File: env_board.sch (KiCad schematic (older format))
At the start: 8 parts, among them J1 CONN_01X07, U1 RFD77101, U2 ENS210, U3 CCS811

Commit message: update schematics
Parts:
- removed R1: 10k, Resistors_SMD:R_0603, symbol R
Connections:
- net BATT_V_EN: now also U1.11 (P0.19); no longer U1.20 (P0.08)
- net CCS_WAKE: now also U1.28 (P0.13)
- net VDD: now also U3.2 (~RESET); no longer J1.3 (P3)
- new net VBUS: J1.3 (P3)
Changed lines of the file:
@@
 $EndComp
 $Comp
-L VDD #PWR09
-U 1 1 599D616B
-P 3100 1900
-F 0 "#PWR09" H 3100 1750 50  0001 C CNN
-F 1 "VDD" H 3100 2050 50  0000 C CNN
-F 2 "" H 3100 1900 50  0001 C CNN
-F 3 "" H 3100 1900 50  0001 C CNN
-	1    3100 1900
-	1    0    0    -1
-$EndComp
-$Comp
-L GND #PWR010
+L GND #PWR09
 U 1 1 599D619D
 P 2550 2250
-F 0 "#PWR010" H 2550 2000 50  0001 C CNN
+F 0 "#PWR09" H 2550 2000 50  0001 C CNN
 F 1 "GND" H 2550 2100 50  0000 C CNN
 F 2 "" H 2550 2250 50  0001 C CNN
@@
 CCS_INT
 Wire Wire Line
-	9300 3050 9200 3050
-Wire Wire Line
-	9200 3050 9200 2750
-Wire Wire Line
 	8900 2750 10400 2750
 Connection ~ 9700 2750
@@
 Text Label 9300 3650 2    60   ~ 0
 CCS_WAKE
-$Comp
-L R R1
-U 1 1 599D70BF
-P 8900 3250
-F 0 "R1" V 8980 3250 50  0000 C CNN
-F 1 "10k" V 8900 3250 50  0000 C CNN
-F 2 "Resistors_SMD:R_0603" V 8830 3250 50  0001 C CNN
-F 3 "" H 8900 3250 50  0001 C CNN
-	1    8900 3250
-	1    0    0    -1
-$EndComp
 Wire Wire Line
-	9300 3550 8900 3550
+	8900 3550 9300 3550
 Wire Wire Line
-	8900 3550 8900 3400
-Wire Wire Line
-	8900 3100 8900 2750
-Connection ~ 9200 2750
+	8900 2750 8900 3550
 NoConn ~ 10100 3450
 $Comp
@@
 $EndComp
 $Comp
-L GND #PWR011
+L GND #PWR010
 U 1 1 599D736D
 P 10400 3050
-F 0 "#PWR011" H 10400 2800 50  0001 C CNN
+F 0 "#PWR010" H 10400 2800 50  0001 C CNN
 F 1 "GND" H 10400 2900 50  0000 C CNN
 F 2 "" H 10400 3050 50  0001 C CNN
@@
 Text Label 2700 3250 0    60   ~ 0
 BATT_V_EN
-Text Label 4050 4350 2    60   ~ 0
+Text Label 5450 4150 0    60   ~ 0
 BATT_V_EN
 Text Label 4050 3850 2    60   ~ 0
@@
 Text Label 4050 3250 2    60   ~ 0
 SWDIO/RESET
+$Comp
+L VBUS #PWR011
+U 1 1 59F89288
+P 3100 1900
+F 0 "#PWR011" H 3100 1750 50  0001 C CNN
+F 1 "VBUS" H 3100 2050 50  0000 C CNN
+F 2 "" H 3100 1900 50  0001 C CNN
+F 3 "" H 3100 1900 50  0001 C CNN
+	1    3100 1900
+	1    0    0    -1
+$EndComp
+Text Label 4050 4850 2    60   ~ 0
+CCS_WAKE
+Wire Wire Line
+	9300 3050 9100 3050
+Wire Wire Line
+	9100 3050 9100 2750
+Connection ~ 9100 2750
 $EndSCHEMATC

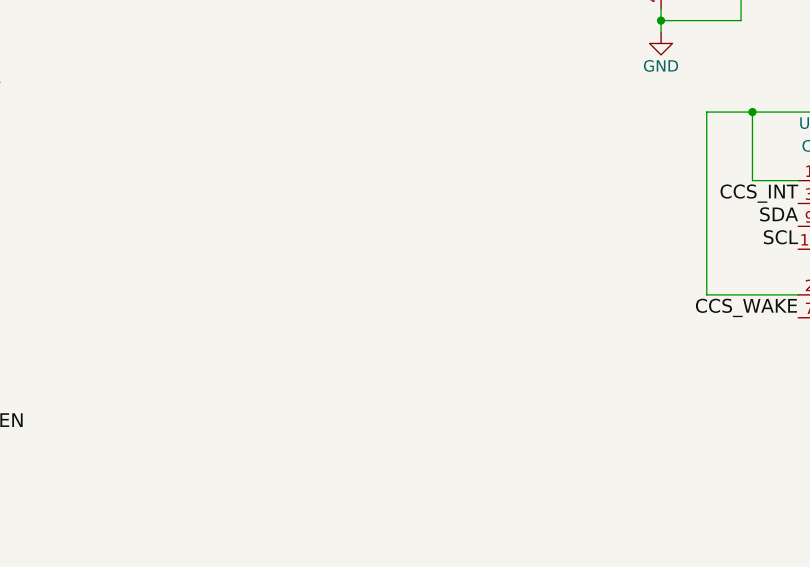
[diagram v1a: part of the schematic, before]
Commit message: update board, schematics, add bmp280
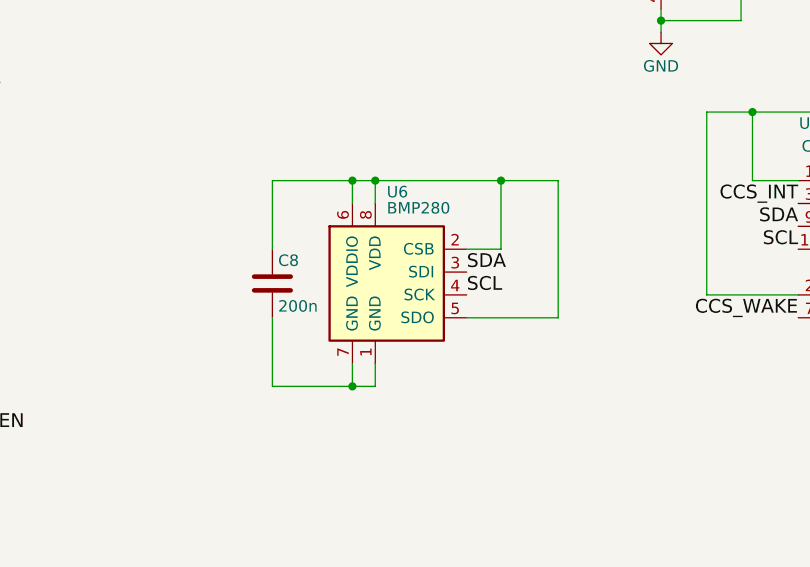
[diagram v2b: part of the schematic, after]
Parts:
- added C8: 200n, Capacitors_SMD:C_0603, symbol C
- added U6: BMP280, Housings_LGA:Bosch_LGA-8_2x2.5mm_Pitch0.65mm, symbol BMP280
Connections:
- net SCL: now also U6.4 (SCK)
- net SDA: now also U6.3 (SDI)
- new net: C8.2, U6.1 (GND), U6.7 (GND)
- new net: C8.1, U6.2 (CSB), U6.5 (SDO), U6.6 (VDDIO), U6.8 (VDD)
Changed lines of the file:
@@
 EESchema Schematic File Version 2
+LIBS:env_board-rescue
 LIBS:power
 LIBS:device
@@
 $EndComp
 $Comp
-L GND #PWR01
+L GND #PWR3
 U 1 1 596DD545
 P 4650 5550
-F 0 "#PWR01" H 4650 5300 50  0001 C CNN
+F 0 "#PWR3" H 4650 5300 50  0001 C CNN
 F 1 "GND" H 4650 5400 50  0000 C CNN
 F 2 "" H 4650 5550 50  0001 C CNN
@@
 $EndComp
 $Comp
-L VDD #PWR02
+L VDD #PWR4
 U 1 1 596DD567
 P 4750 2750
-F 0 "#PWR02" H 4750 2600 50  0001 C CNN
+F 0 "#PWR4" H 4750 2600 50  0001 C CNN
 F 1 "VDD" H 4750 2900 50  0000 C CNN
 F 2 "" H 4750 2750 50  0001 C CNN
@@
 $EndComp
 $Comp
-L VDD #PWR03
+L VDD #PWR5
 U 1 1 596DD6D5
 P 5700 2550
-F 0 "#PWR03" H 5700 2400 50  0001 C CNN
+F 0 "#PWR5" H 5700 2400 50  0001 C CNN
 F 1 "VDD" H 5700 2700 50  0000 C CNN
 F 2 "" H 5700 2550 50  0001 C CNN
@@
 $EndComp
 $Comp
-L GND #PWR04
+L GND #PWR6
 U 1 1 596DD6F2
 P 5700 2850
-F 0 "#PWR04" H 5700 2600 50  0001 C CNN
+F 0 "#PWR6" H 5700 2600 50  0001 C CNN
 F 1 "GND" H 5700 2700 50  0000 C CNN
 F 2 "" H 5700 2850 50  0001 C CNN
@@
 $EndComp
 $Comp
-L VDD #PWR05
+L VDD #PWR7
 U 1 1 599D59B0
 P 8700 1600
-F 0 "#PWR05" H 8700 1450 50  0001 C CNN
+F 0 "#PWR7" H 8700 1450 50  0001 C CNN
 F 1 "VDD" H 8700 1750 50  0000 C CNN
 F 2 "" H 8700 1600 50  0001 C CNN
@@
 $EndComp
 $Comp
-L GND #PWR06
+L GND #PWR8
 U 1 1 599D59DF
 P 8700 2400
-F 0 "#PWR06" H 8700 2150 50  0001 C CNN
+F 0 "#PWR8" H 8700 2150 50  0001 C CNN
 F 1 "GND" H 8700 2250 50  0000 C CNN
 F 2 "" H 8700 2400 50  0001 C CNN
@@
 	8700 2300 8700 2400
 $Comp
-L VDD #PWR07
+L VDD #PWR9
 U 1 1 599D5AF3
 P 9700 2700
-F 0 "#PWR07" H 9700 2550 50  0001 C CNN
+F 0 "#PWR9" H 9700 2550 50  0001 C CNN
 F 1 "VDD" H 9700 2850 50  0000 C CNN
 F 2 "" H 9700 2700 50  0001 C CNN
@@
 $EndComp
 $Comp
-L GND #PWR08
+L GND #PWR10
 U 1 1 599D5B22
 P 9700 3900
-F 0 "#PWR08" H 9700 3650 50  0001 C CNN
+F 0 "#PWR10" H 9700 3650 50  0001 C CNN
 F 1 "GND" H 9700 3750 50  0000 C CNN
 F 2 "" H 9700 3900 50  0001 C CNN
@@
 $EndComp
 $Comp
-L GND #PWR09
+L GND #PWR1
 U 1 1 599D619D
 P 2550 2250
-F 0 "#PWR09" H 2550 2000 50  0001 C CNN
+F 0 "#PWR1" H 2550 2000 50  0001 C CNN
 F 1 "GND" H 2550 2100 50  0000 C CNN
 F 2 "" H 2550 2250 50  0001 C CNN
@@
 $EndComp
 $Comp
-L GND #PWR010
+L GND #PWR11
 U 1 1 599D736D
 P 10400 3050
-F 0 "#PWR010" H 10400 2800 50  0001 C CNN
+F 0 "#PWR11" H 10400 2800 50  0001 C CNN
 F 1 "GND" H 10400 2900 50  0000 C CNN
 F 2 "" H 10400 3050 50  0001 C CNN
@@
 SWDIO/RESET
 $Comp
-L VBUS #PWR011
+L VBUS #PWR2
 U 1 1 59F89288
 P 3100 1900
-F 0 "#PWR011" H 3100 1750 50  0001 C CNN
+F 0 "#PWR2" H 3100 1750 50  0001 C CNN
 F 1 "VBUS" H 3100 2050 50  0000 C CNN
 F 2 "" H 3100 1900 50  0001 C CNN
@@
 	9100 3050 9100 2750
 Connection ~ 9100 2750
+$Comp
+L BMP280 U6
+U 1 1 5A01D7B2
+P 7450 3450
+F 0 "U6" H 7500 3800 50  0000 L CNN
+F 1 "BMP280" H 7500 3700 50  0000 L BNN
+F 2 "Housings_LGA:Bosch_LGA-8_2x2.5mm_Pitch0.65mm" H 7350 3450 50  0001 C CNN
+F 3 "" H 7350 3450 50  0001 C CNN
+	1    7450 3450
+	1    0    0    -1
+$EndComp
+$Comp
+L C C8
+U 1 1 5A01D9B5
+P 7000 3500
+F 0 "C8" H 7025 3600 50  0000 L CNN
+F 1 "200n" H 7025 3400 50  0000 L CNN
+F 2 "Capacitors_SMD:C_0603" H 7038 3350 50  0001 C CNN
+F 3 "" H 7000 3500 50  0001 C CNN
+	1    7000 3500
+	1    0    0    -1
+$EndComp
+Wire Wire Line
+	7000 3350 7000 3050
+Wire Wire Line
+	7000 3050 8250 3050
+Wire Wire Line
+	7450 3050 7450 3150
+Wire Wire Line
+	7350 3150 7350 3050
+Connection ~ 7350 3050
+Wire Wire Line
+	7000 3650 7000 3950
+Wire Wire Line
+	7000 3950 7450 3950
+Wire Wire Line
+	7450 3950 7450 3850
+Wire Wire Line
+	7350 3850 7350 3950
+Connection ~ 7350 3950
+Wire Wire Line
+	7850 3650 8250 3650
+Wire Wire Line
+	8250 3650 8250 3050
+Connection ~ 7450 3050
+Wire Wire Line
+	7850 3350 8000 3350
+Wire Wire Line
+	8000 3350 8000 3050
+Connection ~ 8000 3050
+Text Label 7850 3450 0    60   ~ 0
+SDA
+Text Label 7850 3550 0    60   ~ 0
+SCL
 $EndSCHEMATC

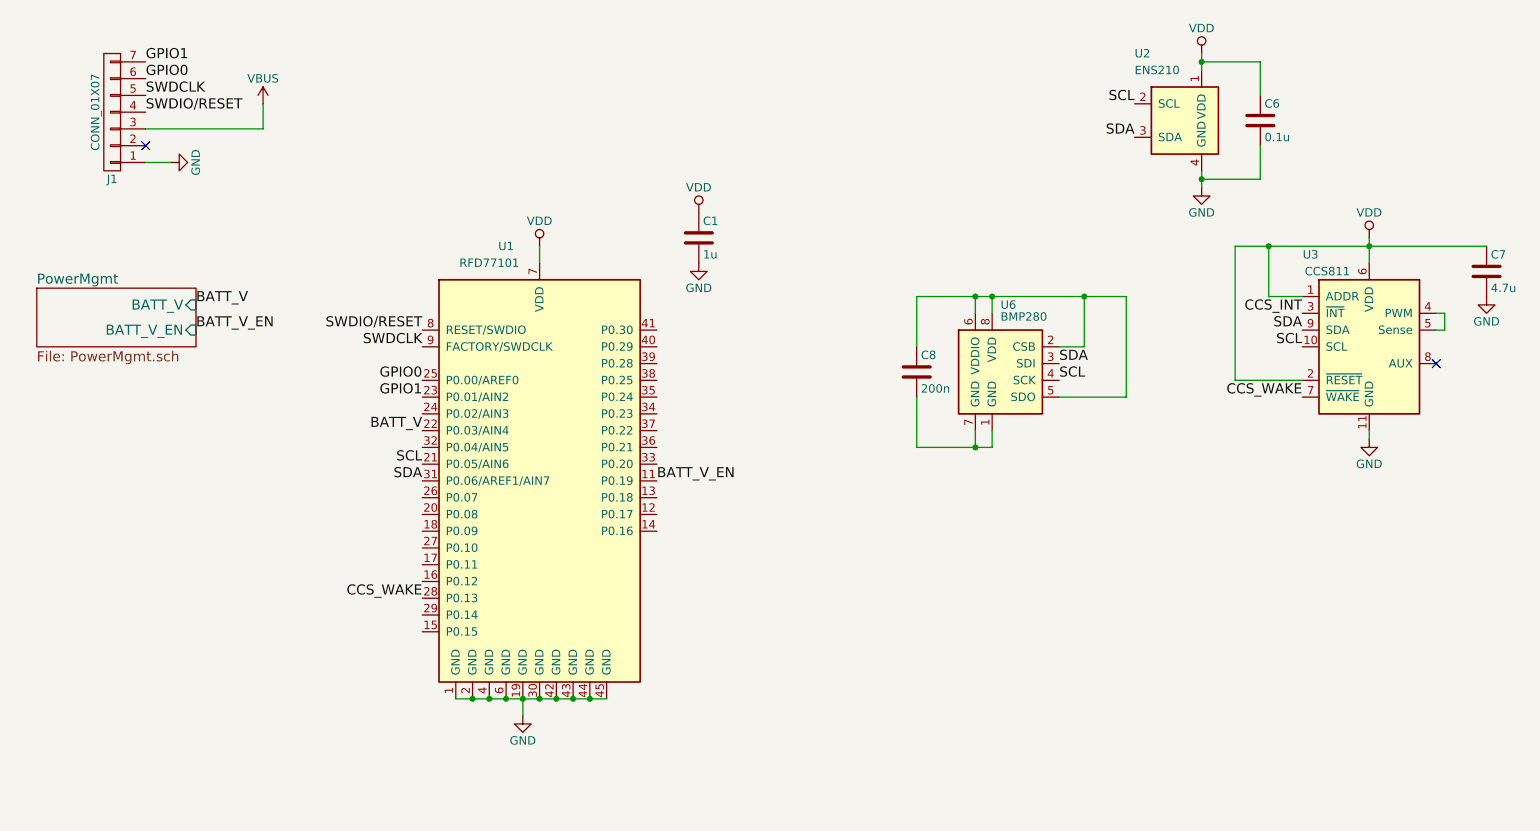
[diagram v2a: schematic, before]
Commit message: update sensor and add housing for sensor
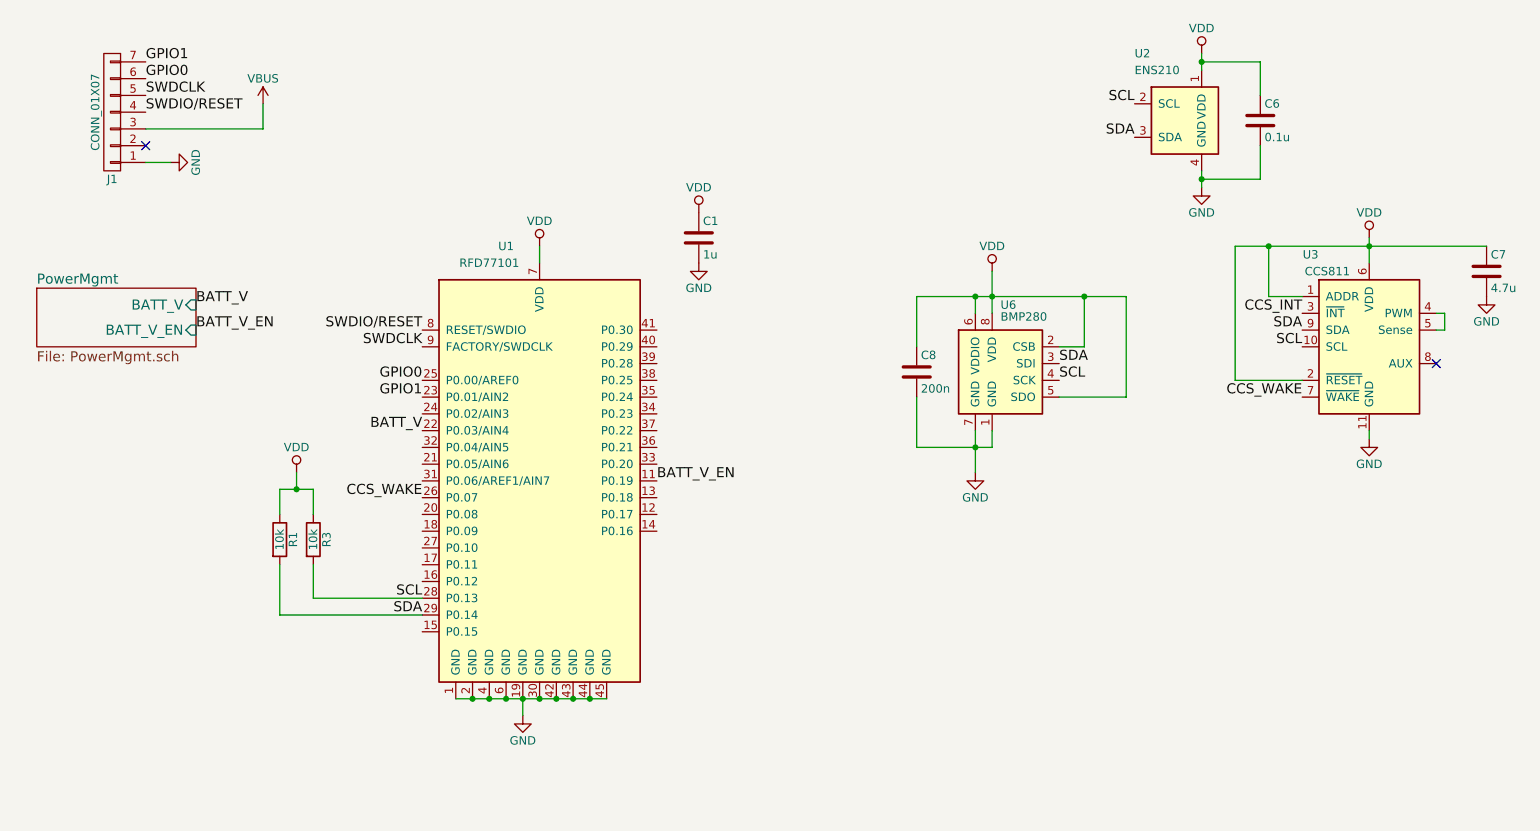
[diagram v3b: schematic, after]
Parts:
- added R1, R3: 10k, Resistors_SMD:R_0603, symbol R
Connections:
- net CCS_WAKE: now also U1.26 (P0.07); no longer U1.28 (P0.13)
- net GND: now also C8.2, U6.1 (GND), U6.7 (GND)
- net SCL: now also U1.28 (P0.13), R3.2; no longer U1.21 (P0.05/AIN6)
- net SDA: now also U1.29 (P0.14), R1.2; no longer U1.31 (P0.06/AREF1/AIN7)
- net VDD: now also C8.1, U6.2 (CSB), U6.5 (SDO), U6.6 (VDDIO), U6.8 (VDD), R1.1, R3.1
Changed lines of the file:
@@
 LIBS:rfcom
 LIBS:sensors
-LIBS:Battery_Management
 LIBS:env_board-cache
 EELAYER 25 0
@@
 $EndComp
 $Comp
-L GND #PWR3
+L GND #PWR01
 U 1 1 596DD545
 P 4650 5550
-F 0 "#PWR3" H 4650 5300 50  0001 C CNN
+F 0 "#PWR01" H 4650 5300 50  0001 C CNN
 F 1 "GND" H 4650 5400 50  0000 C CNN
 F 2 "" H 4650 5550 50  0001 C CNN
@@
 $EndComp
 $Comp
-L VDD #PWR4
+L VDD #PWR02
 U 1 1 596DD567
 P 4750 2750
-F 0 "#PWR4" H 4750 2600 50  0001 C CNN
+F 0 "#PWR02" H 4750 2600 50  0001 C CNN
 F 1 "VDD" H 4750 2900 50  0000 C CNN
 F 2 "" H 4750 2750 50  0001 C CNN
@@
 $EndComp
 $Comp
-L VDD #PWR5
+L VDD #PWR03
 U 1 1 596DD6D5
 P 5700 2550
-F 0 "#PWR5" H 5700 2400 50  0001 C CNN
+F 0 "#PWR03" H 5700 2400 50  0001 C CNN
 F 1 "VDD" H 5700 2700 50  0000 C CNN
 F 2 "" H 5700 2550 50  0001 C CNN
@@
 $EndComp
 $Comp
-L GND #PWR6
+L GND #PWR04
 U 1 1 596DD6F2
 P 5700 2850
-F 0 "#PWR6" H 5700 2600 50  0001 C CNN
+F 0 "#PWR04" H 5700 2600 50  0001 C CNN
 F 1 "GND" H 5700 2700 50  0000 C CNN
 F 2 "" H 5700 2850 50  0001 C CNN
@@
 $EndComp
 $Comp
-L VDD #PWR7
+L VDD #PWR05
 U 1 1 599D59B0
 P 8700 1600
-F 0 "#PWR7" H 8700 1450 50  0001 C CNN
+F 0 "#PWR05" H 8700 1450 50  0001 C CNN
 F 1 "VDD" H 8700 1750 50  0000 C CNN
 F 2 "" H 8700 1600 50  0001 C CNN
@@
 $EndComp
 $Comp
-L GND #PWR8
+L GND #PWR06
 U 1 1 599D59DF
 P 8700 2400
-F 0 "#PWR8" H 8700 2150 50  0001 C CNN
+F 0 "#PWR06" H 8700 2150 50  0001 C CNN
 F 1 "GND" H 8700 2250 50  0000 C CNN
 F 2 "" H 8700 2400 50  0001 C CNN
@@
 	8700 2300 8700 2400
 $Comp
-L VDD #PWR9
+L VDD #PWR07
 U 1 1 599D5AF3
 P 9700 2700
-F 0 "#PWR9" H 9700 2550 50  0001 C CNN
+F 0 "#PWR07" H 9700 2550 50  0001 C CNN
 F 1 "VDD" H 9700 2850 50  0000 C CNN
 F 2 "" H 9700 2700 50  0001 C CNN
@@
 $EndComp
 $Comp
-L GND #PWR10
+L GND #PWR08
 U 1 1 599D5B22
 P 9700 3900
-F 0 "#PWR10" H 9700 3650 50  0001 C CNN
+F 0 "#PWR08" H 9700 3650 50  0001 C CNN
 F 1 "GND" H 9700 3750 50  0000 C CNN
 F 2 "" H 9700 3900 50  0001 C CNN
@@
 $EndComp
 $Comp
-L GND #PWR1
+L GND #PWR09
 U 1 1 599D619D
 P 2550 2250
-F 0 "#PWR1" H 2550 2000 50  0001 C CNN
+F 0 "#PWR09" H 2550 2000 50  0001 C CNN
 F 1 "GND" H 2550 2100 50  0000 C CNN
 F 2 "" H 2550 2250 50  0001 C CNN
@@
 Text Label 4050 3650 2    60   ~ 0
 GPIO1
-Text Label 4050 4150 2    60   ~ 0
+Text Label 4050 4950 2    60   ~ 0
 SDA
-Text Label 4050 4050 2    60   ~ 0
+Text Label 4050 4850 2    60   ~ 0
 SCL
 Text Label 8300 2100 2    60   ~ 0
@@
 $EndComp
 $Comp
-L GND #PWR11
+L GND #PWR010
 U 1 1 599D736D
 P 10400 3050
-F 0 "#PWR11" H 10400 2800 50  0001 C CNN
+F 0 "#PWR010" H 10400 2800 50  0001 C CNN
 F 1 "GND" H 10400 2900 50  0000 C CNN
 F 2 "" H 10400 3050 50  0001 C CNN
@@
 SWDIO/RESET
 $Comp
-L VBUS #PWR2
+L VBUS #PWR011
 U 1 1 59F89288
 P 3100 1900
-F 0 "#PWR2" H 3100 1750 50  0001 C CNN
+F 0 "#PWR011" H 3100 1750 50  0001 C CNN
 F 1 "VBUS" H 3100 2050 50  0000 C CNN
 F 2 "" H 3100 1900 50  0001 C CNN
@@
 	1    0    0    -1
 $EndComp
-Text Label 4050 4850 2    60   ~ 0
+Text Label 4050 4250 2    60   ~ 0
 CCS_WAKE
 Wire Wire Line
@@
 	7000 3050 8250 3050
 Wire Wire Line
-	7450 3050 7450 3150
+	7450 2900 7450 3150
 Wire Wire Line
 	7350 3150 7350 3050
@@
 	7450 3950 7450 3850
 Wire Wire Line
-	7350 3850 7350 3950
+	7350 3850 7350 4100
 Connection ~ 7350 3950
 Wire Wire Line
@@
 Text Label 7850 3550 0    60   ~ 0
 SCL
+$Comp
+L VDD #PWR012
+U 1 1 5A71A152
+P 7450 2900
+F 0 "#PWR012" H 7450 2750 50  0001 C CNN
+F 1 "VDD" H 7450 3050 50  0000 C CNN
+F 2 "" H 7450 2900 50  0001 C CNN
+F 3 "" H 7450 2900 50  0001 C CNN
+	1    7450 2900
+	1    0    0    -1
+$EndComp
+$Comp
+L GND #PWR013
+U 1 1 5A71A1C7
+P 7350 4100
+F 0 "#PWR013" H 7350 3850 50  0001 C CNN
+F 1 "GND" H 7350 3950 50  0000 C CNN
+F 2 "" H 7350 4100 50  0001 C CNN
+F 3 "" H 7350 4100 50  0001 C CNN
+	1    7350 4100
+	1    0    0    -1
+$EndComp
+$Comp
+L R R3
+U 1 1 5A9016EB
+P 3400 4500
+F 0 "R3" V 3480 4500 50  0000 C CNN
+F 1 "10k" V 3400 4500 50  0000 C CNN
+F 2 "Resistors_SMD:R_0603" V 3330 4500 50  0001 C CNN
+F 3 "" H 3400 4500 50  0000 C CNN
+	1    3400 4500
+	1    0    0    -1
+$EndComp
+$Comp
+L R R1
+U 1 1 5A90189B
+P 3200 4500
+F 0 "R1" V 3280 4500 50  0000 C CNN
+F 1 "10k" V 3200 4500 50  0000 C CNN
+F 2 "Resistors_SMD:R_0603" V 3130 4500 50  0001 C CNN
+F 3 "" H 3200 4500 50  0000 C CNN
+	1    3200 4500
+	1    0    0    -1
+$EndComp
+Wire Wire Line
+	4050 4950 3200 4950
+Wire Wire Line
+	3200 4950 3200 4650
+Wire Wire Line
+	4050 4850 3400 4850
+Wire Wire Line
+	3400 4850 3400 4650
+$Comp
+L VDD #PWR014
+U 1 1 5A901B29
+P 3300 4100
+F 0 "#PWR014" H 3300 3950 50  0001 C CNN
+F 1 "VDD" H 3300 4250 50  0000 C CNN
+F 2 "" H 3300 4100 50  0001 C CNN
+F 3 "" H 3300 4100 50  0001 C CNN
+	1    3300 4100
+	1    0    0    -1
+$EndComp
+Wire Wire Line
+	3200 4350 3200 4200
+Wire Wire Line
+	3200 4200 3400 4200
+Wire Wire Line
+	3300 4200 3300 4100
+Wire Wire Line
+	3400 4200 3400 4350
+Connection ~ 3300 4200
 $EndSCHEMATC

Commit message: update sensor/housings
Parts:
- added R4: 10k, Resistor_SMD:R_0603_1608Metric, symbol Device:R
- C1, C6, C7, C8: footprint Capacitors_SMD:C_0603 -> Capacitor_SMD:C_0603_1608Metric; symbol C -> Device:C
- J1: footprint Pin_Headers:Pin_Header_Straight_1x07_Pitch2.54mm -> Connector_PinHeader_2.54mm:PinHeader_1x07_P2.54mm_Vertical; symbol CONN_01X07 -> Connector_Generic:Conn_01x07
- R1, R3: footprint Resistors_SMD:R_0603 -> Resistor_SMD:R_0603_1608Metric; symbol R -> Device:R
- U1: footprint kicad-RF_Modules:RFDigital_RFD77101 -> RF_Module:RFDigital_RFD77101; symbol RFD77101 -> RF_Bluetooth:RFD77101
- U2: footprint Housings_DFN_QFN:AMS_QFN-4-1EP_2x2mm_Pitch0.95mm -> Package_DFN_QFN:AMS_QFN-4-1EP_2x2mm_P0.95mm_EP0.7x1.6mm; symbol ENS210 -> Sensor_Humidity:ENS210
- U3: footprint kicad-Housings_LGA:AMS_LGA-10-1EP_2.7x4mm_Pitch0.6mm -> Package_LGA:AMS_LGA-10-1EP_2.7x4mm_P0.6mm; symbol CCS811 -> Sensor_Gas:CCS811
- U6: footprint Housings_LGA:Bosch_LGA-8_2x2.5mm_Pitch0.65mm -> Package_LGA:Bosch_LGA-8_2x2.5mm_P0.65mm_ClockwisePinNumbering; symbol BMP280 -> env_board-rescue:BMP280-Sensor_Pressure
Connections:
- wire segments 42 -> 61
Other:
- moved on the sheet: C8
